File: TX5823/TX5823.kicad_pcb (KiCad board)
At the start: 4 copper layers, 92 parts, among them IC1 ATMEGA328P-A, IC2 ATTINY13A-SS, P1 Akku_in, P2 ISP, P3 Mavlink, P4 CONN_01X01, P5 CONN_01X01, P6 CONN_01X01, P7 CONN_01X01, Q1 MOSFET_P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

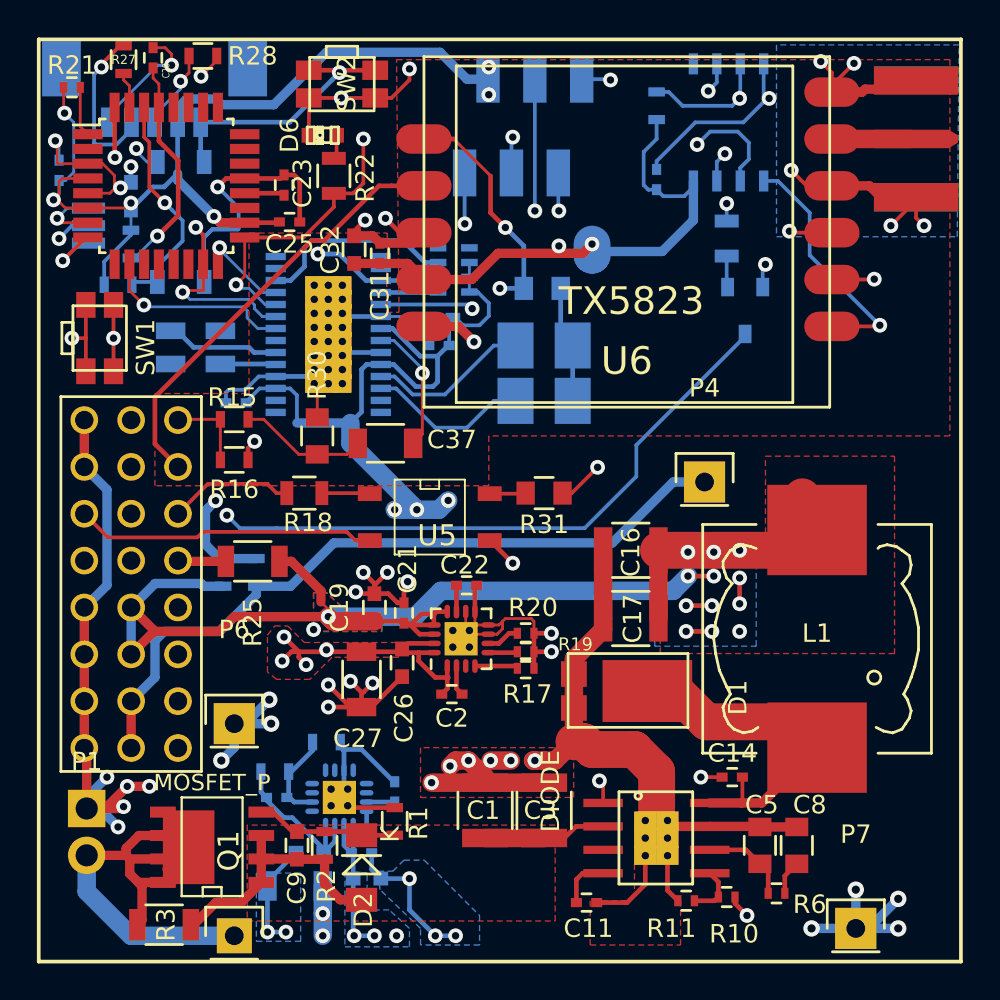
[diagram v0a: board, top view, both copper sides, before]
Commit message: DSBGA(&) Footprint für Löttests hinzugefügt. Keine relevanz für diese Platine
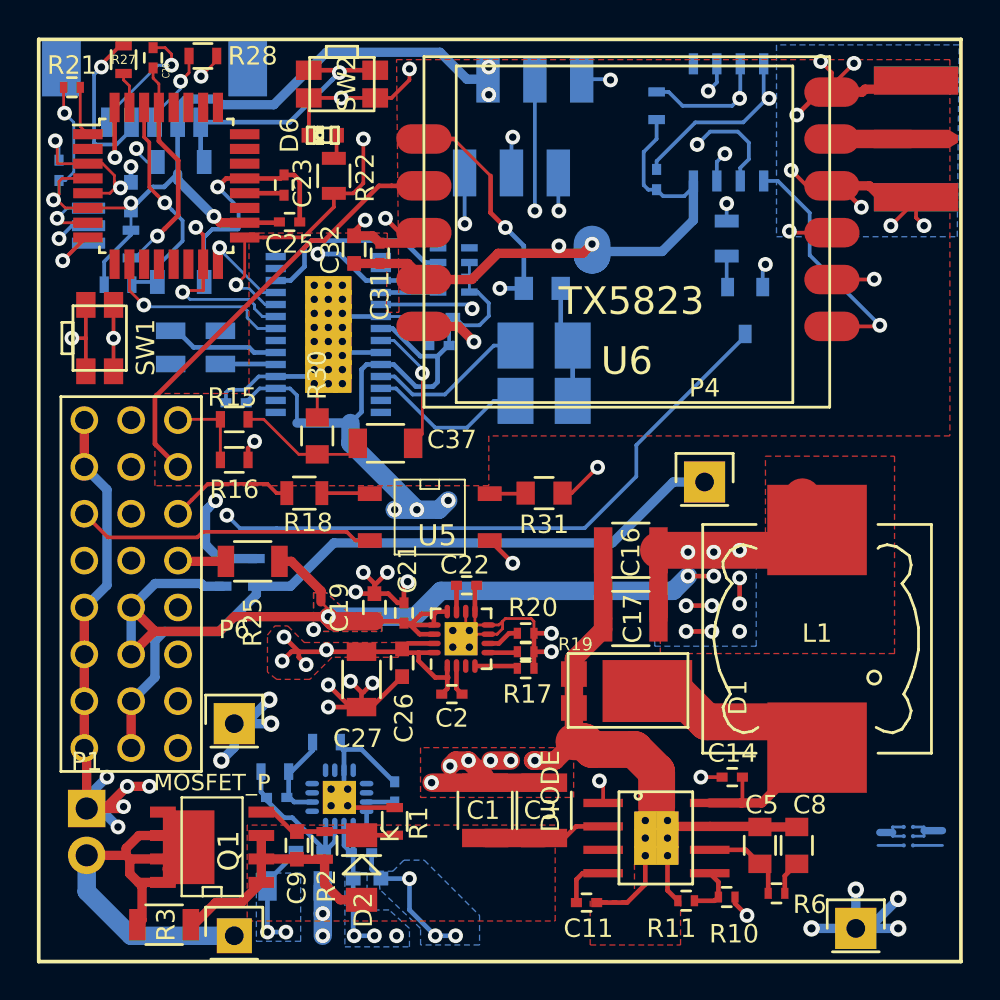
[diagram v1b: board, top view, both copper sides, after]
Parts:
- added U9: TPS22963, toni:DSBGS(6), B.Cu at (121.9, 62.7)
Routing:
- net GND: track 295.9 -> 301.4 mm, vias 53 -> 55
- net Net-(U9-PadA1): track 0.00 -> 2.70 mm
- net Net-(U9-PadA2): track 0.00 -> 2.50 mm
- net Net-(U9-PadC1): track 0.00 -> 1.60 mm
- net Net-(U9-PadC2): track 0.00 -> 1.40 mm
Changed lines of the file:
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@@
 (kicad_pcb (version 4) (host pcbnew "(2014-10-31 BZR 5243)-product")
   (general
-    (links 272)
+    (links 274)
     (no_connects 0)
     (area 66.784999 16.636 137.520543 71.265)
     (thickness 1.6)
     (drawings 4)
-    (tracks 1110)
+    (tracks 1130)
     (zones 0)
-    (modules 92)
-    (nets 109)
+    (modules 93)
+    (nets 113)
   )
   (page A4)
@@
   )
   (setup
-    (last_trace_width 0.254)
+    (last_trace_width 0.4)
     (user_trace_width 0.1524)
     (user_trace_width 0.16)
@@
   (net 107 "Net-(U1-Pad10)")
   (net 108 "Net-(U1-Pad1)")
+  (net 109 "Net-(U9-PadA2)")
+  (net 110 "Net-(U9-PadA1)")
+  (net 111 "Net-(U9-PadC1)")
+  (net 112 "Net-(U9-PadC2)")
   (net_class Default "Dies ist die voreingestellte Netzklasse."
     (clearance 0.19)
@@
     (add_net "Net-(U7-Pad5)")
     (add_net "Net-(U7-Pad6)")
+    (add_net "Net-(U9-PadA1)")
+    (add_net "Net-(U9-PadA2)")
+    (add_net "Net-(U9-PadC1)")
+    (add_net "Net-(U9-PadC2)")
   )
   (module Socket_Strips:Socket_Strip_Angled_1x02 (layer F.Cu)
@@
     (descr "Through hole pin header")
     (tags "pin header")
-    (fp_text reference P7 (at 0 -5.1) (layer F.SilkS)
+    (fp_text reference P7 (at 0 -5.1) (layer F.SilkS) hide
       (effects (font (size 1 1) (thickness 0.15)))
     )
@@
     )
   )
+  (module "toni:DSBGS(6)" (layer B.Cu)
+    (at 121.9 62.7)
+    (fp_text reference U9 (at 0.254 4.445) (layer B.SilkS)
+      (effects (font (size 1.5 1.5) (thickness 0.15)) (justify mirror))
+    )
+    (fp_text value TPS22963 (at 1.016 6.604) (layer B.SilkS) hide
+      (effects (font (size 1.5 1.5) (thickness 0.15)) (justify mirror))
+    )
+    (fp_line (start -0.25 -0.25) (end 0.75 -0.25) (layer B.SilkS) (width 0.05))
+    (fp_line (start 0.75 -0.25) (end 0.75 1.25) (layer B.SilkS) (width 0.05))
+    (fp_line (start 0.75 1.25) (end -0.25 1.25) (layer B.SilkS) (width 0.05))
+    (fp_line (start -0.25 1.25) (end -0.25 -0.25) (layer B.SilkS) (width 0.05))
+    (pad A2 smd circle (at 0 0) (size 0.225 0.225) (layers B.Cu B.Paste B.Mask)
+      (net 109 "Net-(U9-PadA2)") (solder_mask_margin 0.06))
+    (pad A1 smd circle (at 0.5 0) (size 0.225 0.225) (layers B.Cu B.Paste B.Mask)
+      (net 110 "Net-(U9-PadA1)") (solder_mask_margin 0.06))
+    (pad B2 smd circle (at 0 0.5) (size 0.225 0.225) (layers B.Cu B.Paste B.Mask)
+      (net 109 "Net-(U9-PadA2)") (solder_mask_margin 0.06))
+    (pad B1 smd circle (at 0.5 0.5) (size 0.225 0.225) (layers B.Cu B.Paste B.Mask)
+      (net 110 "Net-(U9-PadA1)") (solder_mask_margin 0.06))
+    (pad C1 smd circle (at 0.5 1) (size 0.225 0.225) (layers B.Cu B.Paste B.Mask)
+      (net 111 "Net-(U9-PadC1)") (solder_mask_margin 0.06))
+    (pad C2 smd circle (at 0 1) (size 0.225 0.225) (layers B.Cu B.Paste B.Mask)
+      (net 112 "Net-(U9-PadC2)") (solder_mask_margin 0.06))
+  )
   (gr_line (start 125 70) (end 75 70) (angle 90) (layer F.SilkS) (width 0.2))
   (gr_line (start 125 20) (end 125 70) (angle 90) (layer F.SilkS) (width 0.2))
@@
   (via (at 84.9 59.1) (size 0.889) (layers F.Cu B.Cu) (net 2))
   (segment (start 85.6 57.1) (end 85.6 58.4) (width 0.508) (layer B.Cu) (net 2))
+  (segment (start 118.005 27.94) (end 118.96 27.94) (width 0.254) (layer F.Cu) (net 2))
+  (via (at 119.6 29.1) (size 0.8) (drill 0.4) (layers F.Cu B.Cu) (net 2))
+  (segment (start 118.44 27.94) (end 119.6 29.1) (width 0.254) (layer F.Cu) (net 2))
+  (segment (start 118.005 27.94) (end 118.44 27.94) (width 0.254) (layer F.Cu) (net 2))
+  (via (at 116.1 24.1) (size 0.8) (drill 0.4) (layers F.Cu B.Cu) (net 2))
+  (segment (start 117.34 22.86) (end 116.1 24.1) (width 0.254) (layer F.Cu) (net 2))
+  (segment (start 118.005 22.86) (end 117.34 22.86) (width 0.254) (layer F.Cu) (net 2))
   (segment (start 114.55 66.3) (end 114.55 65.15) (width 0.254) (layer F.Cu) (net 3))
   (segment (start 114.55 65.15) (end 114.1 64.7) (width 0.254) (layer F.Cu) (net 3))
@@
   (segment (start 84.187885 44.609218) (end 84.587884 45.009217) (width 0.508) (layer Signal) (net 13))
   (segment (start 85 48.15) (end 86.8 48.15) (width 0.508) (layer B.Cu) (net 13))
-  (segment (start 87.2 40.6) (end 89.1 42.5) (width 0.16) (layer F.Cu) (net 14))
+  (segment (start 87.2 40.6) (end 89.1 42.5) (width 0.1524) (layer F.Cu) (net 14))
   (segment (start 89.1 42.5) (end 90.1 42.5) (width 0.16) (layer F.Cu) (net 14))
-  (segment (start 86.35 40.6) (end 87.2 40.6) (width 0.16) (layer F.Cu) (net 14))
-  (segment (start 90.1 42.5) (end 91.7 42.5) (width 0.16) (layer F.Cu) (net 14))
-  (segment (start 91.7 42.5) (end 92.3 41.9) (width 0.16) (layer F.Cu) (net 14))
+  (segment (start 86.35 40.6) (end 87.2 40.6) (width 0.1524) (layer F.Cu) (net 14))
+  (segment (start 92.3 42.5) (end 92.3 41.9) (width 0.1524) (layer F.Cu) (net 14))
+  (segment (start 90.1 42.5) (end 92.3 42.5) (width 0.1524) (layer F.Cu) (net 14))
   (segment (start 84.85 40.6) (end 84.85 42.8) (width 0.16) (layer F.Cu) (net 15))
-  (segment (start 84.85 40.6) (end 82.59 40.6) (width 0.16) (layer F.Cu) (net 15))
+  (segment (start 84.85 40.6) (end 82.59 40.6) (width 0.1524) (layer F.Cu) (net 15))
   (segment (start 82.59 40.6) (end 82.55 40.64) (width 0.508) (layer F.Cu) (net 15))
   (segment (start 86.35 42.8) (end 86.35 42.15) (width 0.254) (layer F.Cu) (net 16))
@@
   (via (at 95.8 38.1) (size 0.8) (drill 0.4) (layers F.Cu B.Cu) (net 57))
   (segment (start 95.8 41.4) (end 95.3 41.9) (width 0.16) (layer F.Cu) (net 57))
-  (segment (start 95.8 38.1) (end 95.8 41.4) (width 0.16) (layer F.Cu) (net 57))
+  (segment (start 95.8 38.1) (end 95.8 41.4) (width 0.1524) (layer F.Cu) (net 57))
   (segment (start 112.3 31.75) (end 112.3 33.3825) (width 0.2032) (layer B.Cu) (net 73))
   (segment (start 112.3 33.3825) (end 112.3475 33.43) (width 0.2032) (layer B.Cu) (net 73))
@@
   (segment (start 88.6 61.1) (end 88.85 61.35) (width 0.254) (layer B.Cu) (net 100))
   (segment (start 88.85 61.35) (end 89.825 61.35) (width 0.254) (layer B.Cu) (net 100))
+  (segment (start 120.5 63) (end 120.6 63) (width 0.1524) (layer B.Cu) (net 109))
+  (segment (start 120.6 63) (end 121.3 63) (width 0.4) (layer B.Cu) (net 109))
+  (segment (start 121.9 62.7) (end 121.3 62.7) (width 0.1524) (layer B.Cu) (net 109) (status 400000))
+  (segment (start 121.3 63.2) (end 121.9 63.2) (width 0.1524) (layer B.Cu) (net 109) (status 800000))
+  (segment (start 121.3 62.7) (end 121.3 63) (width 0.1524) (layer B.Cu) (net 109))
+  (segment (start 121.3 63) (end 121.3 63.2) (width 0.1524) (layer B.Cu) (net 109))
+  (segment (start 123 62.9) (end 124 62.9) (width 0.4) (layer B.Cu) (net 110))
+  (segment (start 122.4 62.7) (end 123 62.7) (width 0.1524) (layer B.Cu) (net 110) (status 400000))
+  (segment (start 123 63.2) (end 122.4 63.2) (width 0.1524) (layer B.Cu) (net 110) (status 800000))
+  (segment (start 123 62.7) (end 123 62.9) (width 0.1524) (layer B.Cu) (net 110))
+  (segment (start 123 62.9) (end 123 63.2) (width 0.1524) (layer B.Cu) (net 110))
+  (segment (start 122.4 63.7) (end 124 63.7) (width 0.1524) (layer B.Cu) (net 111) (status 400000))
+  (segment (start 121.9 63.7) (end 120.5 63.7) (width 0.1524) (layer B.Cu) (net 112) (status 400000))
   (zone (net 97) (net_name /5,2V) (layer F.Cu) (hatch edge 0.508)
     (connect_pads yes (clearance 0.6))
